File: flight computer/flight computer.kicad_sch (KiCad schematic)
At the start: 16 parts, among them U1 TPS56A37RPAR

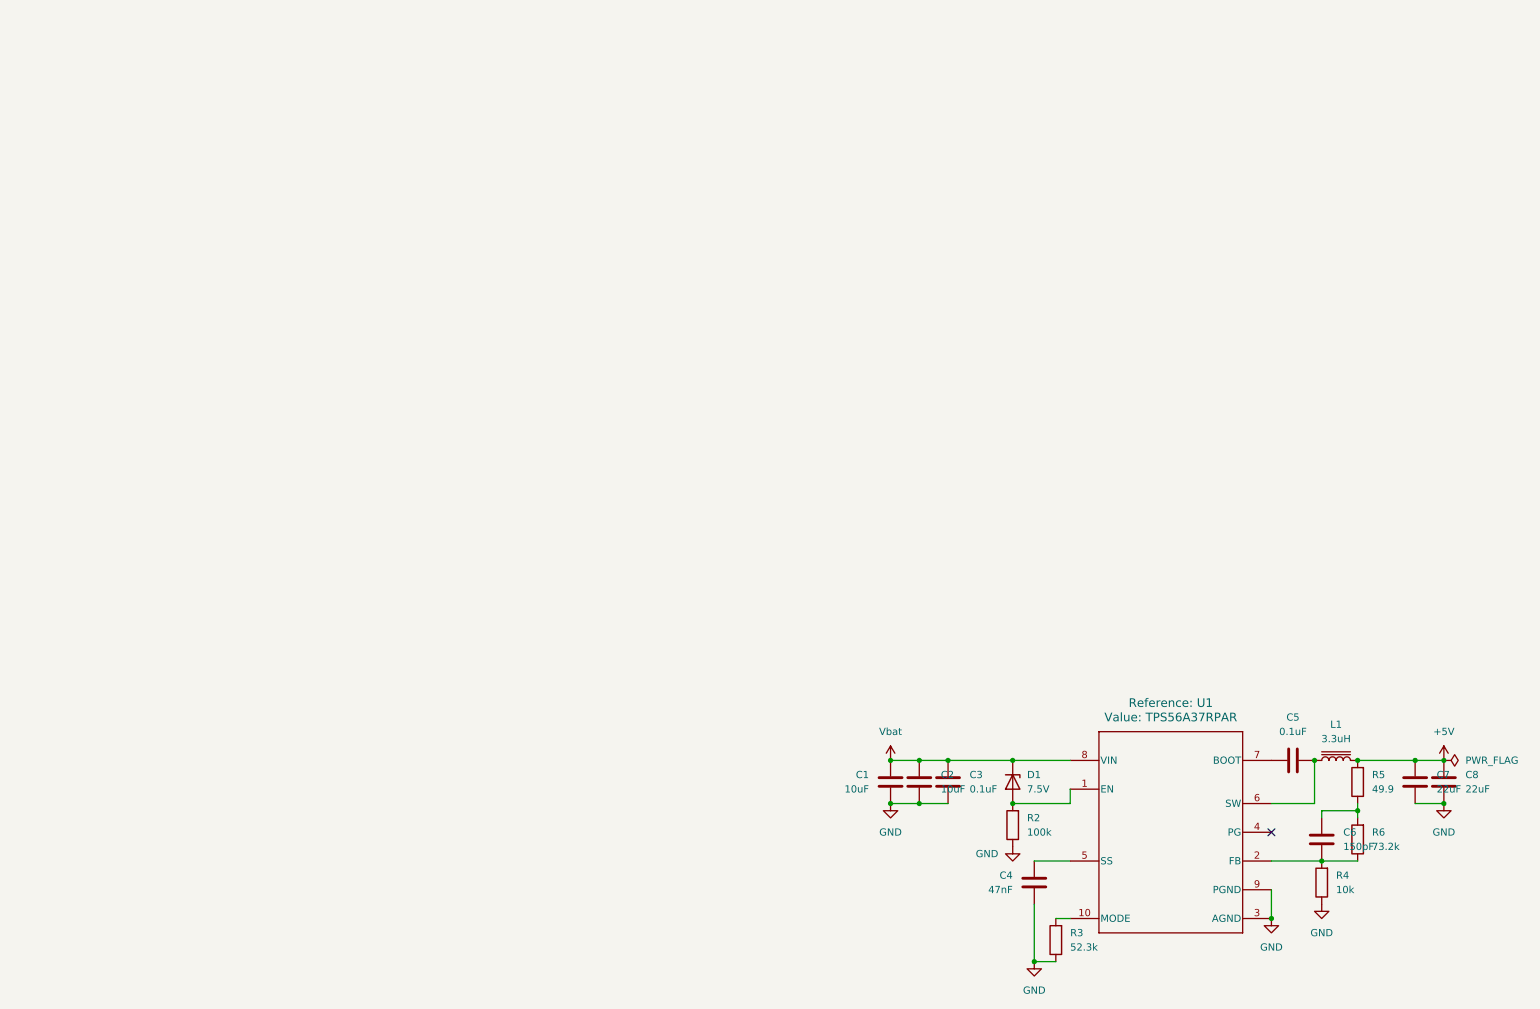
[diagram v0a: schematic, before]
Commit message: BMP581 barometer added
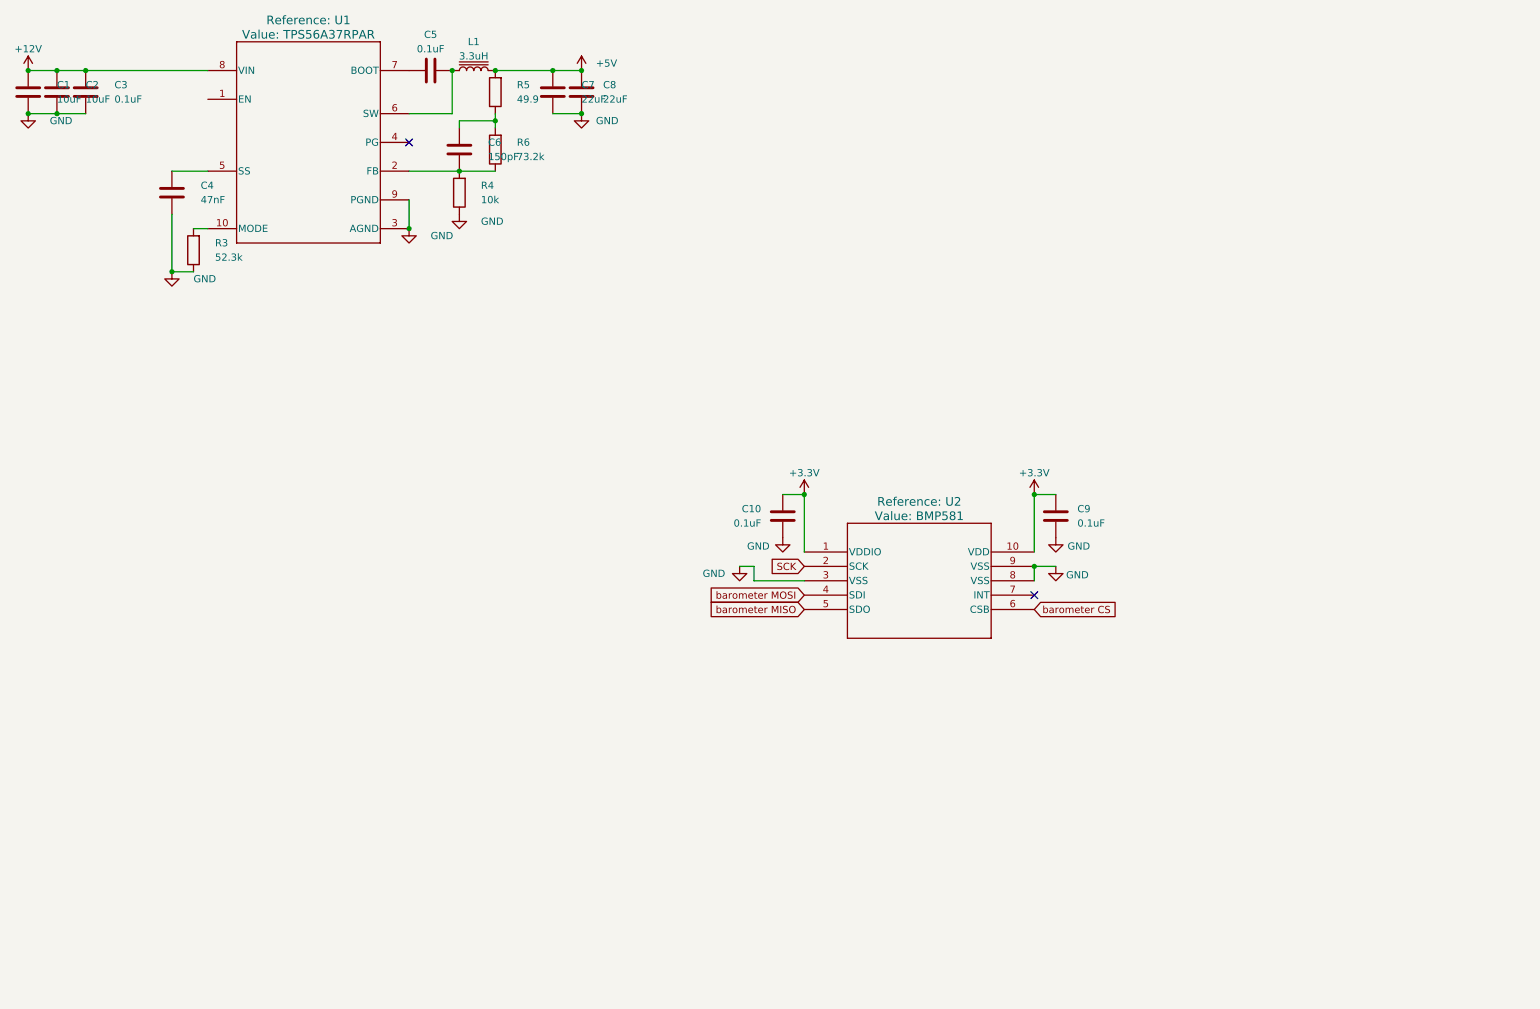
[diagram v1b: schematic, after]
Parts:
- removed D1: 7.5V, symbol Device:D_Zener
- removed R2: 100k, Resistor_SMD:R_0805_2012Metric_Pad1.20x1.40mm_HandSolder, symbol Device:R
- added C10, C9: 0.1uF, Capacitor_SMD:C_0805_2012Metric_Pad1.18x1.45mm_HandSolder, symbol Device:C
- added U2: BMP581, Snapeda:QFN10_BMP581_BOS-L, symbol Snapeda:BMP581
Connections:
- net GND: now also C10.2, C9.2, U2.3 (VSS), U2.8 (VSS), U2.9 (VSS)
- net Vbat renamed +12V
- new net +3.3V: C10.1, C9.1, U2.1 (VDDIO), U2.10 (VDD)
- new net SCK: U2.2 (SCK)
- new net barometer CS: U2.6 (CSB)
- new net barometer MISO: U2.5 (SDO)
- new net barometer MOSI: U2.4 (SDI)
- no-connect marks 1 -> 2
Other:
- moved on the sheet: C1, C2, C3, C4, C5, C6, C7, C8, L1, R3, R4, R5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

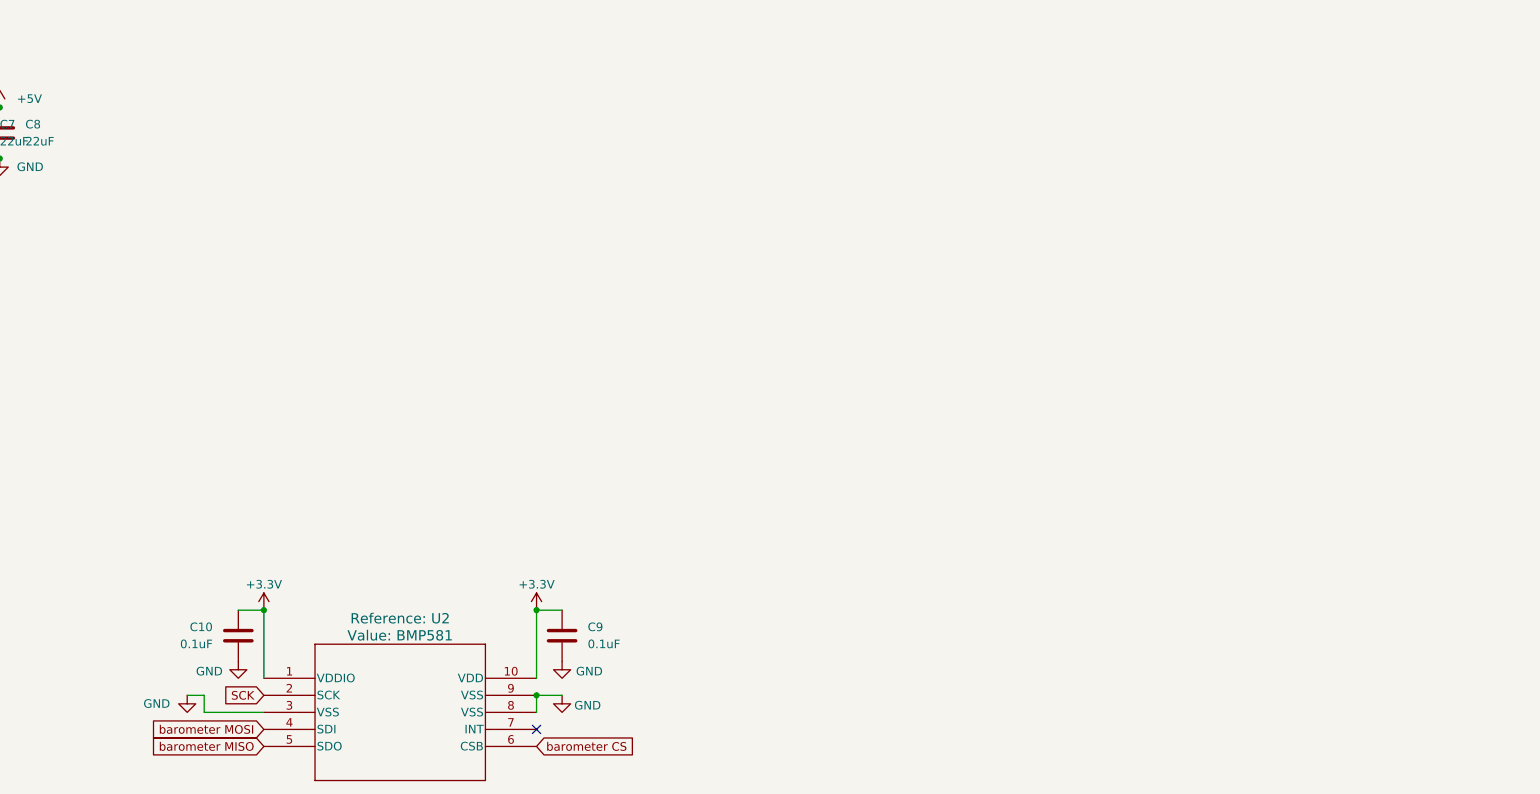
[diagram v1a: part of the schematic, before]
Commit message: BNO086 IMU added
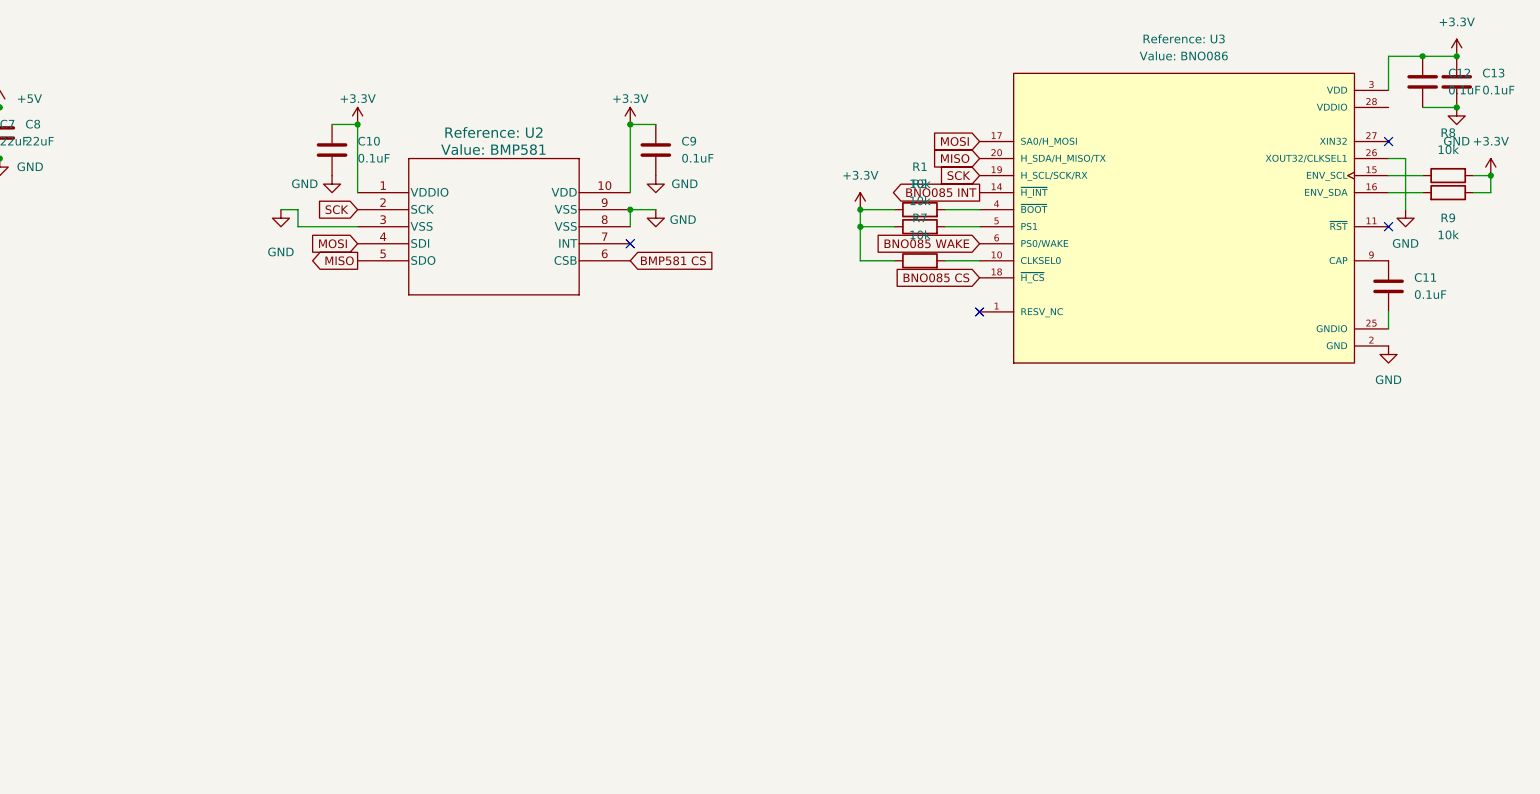
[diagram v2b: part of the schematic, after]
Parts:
- added C11, C12, C13: 0.1uF, Capacitor_SMD:C_0805_2012Metric_Pad1.18x1.45mm_HandSolder, symbol Device:C
- added R1, R2, R7, R8, R9: 10k, Resistor_SMD:R_0805_2012Metric_Pad1.20x1.40mm_HandSolder, symbol Device:R
- added U3: BNO086, Snapeda:IC_BNO086, symbol Snapeda:BNO086
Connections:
- net +3.3V: now also C12.1, C13.1, R1.1, R2.1, R7.1, R8.2, R9.1, U3.3 (VDD)
- net GND: now also C12.2, C13.2, U3.2 (GND), U3.26 (XOUT32/CLKSEL1)
- net SCK: now also U3.19 (H_SCL/SCK/RX)
- net barometer CS renamed BMP581 CS
- net barometer MISO renamed MISO
- net MISO: now also U3.20 (H_SDA/H_MISO/TX)
- net barometer MOSI renamed MOSI
- net MOSI: now also U3.17 (SA0/H_MOSI)
- new net: R7.2, U3.10 (CLKSEL0)
- new net: R2.2, U3.5 (PS1)
- new net: C11.1, U3.9 (CAP)
- new net: C11.2, U3.25 (GNDIO)
- new net: R9.2, U3.16 (ENV_SDA)
- new net: U3.1 (RESV_NC), U3.12 (RESV_NC), U3.13 (RESV_NC), U3.21 (RESV_NC), U3.22 (RESV_NC), U3.23 (RESV_NC), U3.24 (RESV_NC), U3.7 (RESV_NC), U3.8 (RESV_NC)
- new net: R8.1, U3.15 (ENV_SCL)
- new net: R1.2, U3.4 (~{BOOT})
- new net BNO085 CS: U3.18 (~{H_CS})
- new net BNO085 INT: U3.14 (~{H_INT})
- new net BNO085 WAKE: U3.6 (PS0/WAKE)
- no-connect marks 2 -> 5
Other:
- moved on the sheet: C10, C9, Reference: U2

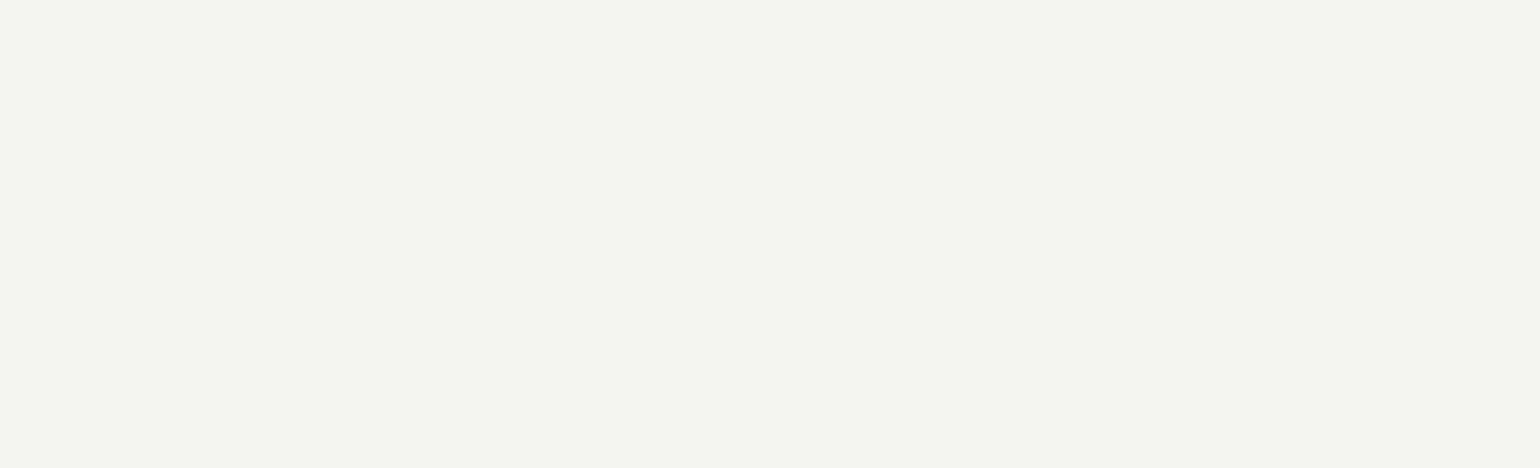
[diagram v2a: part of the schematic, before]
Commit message: BTM9011EP motor controller added
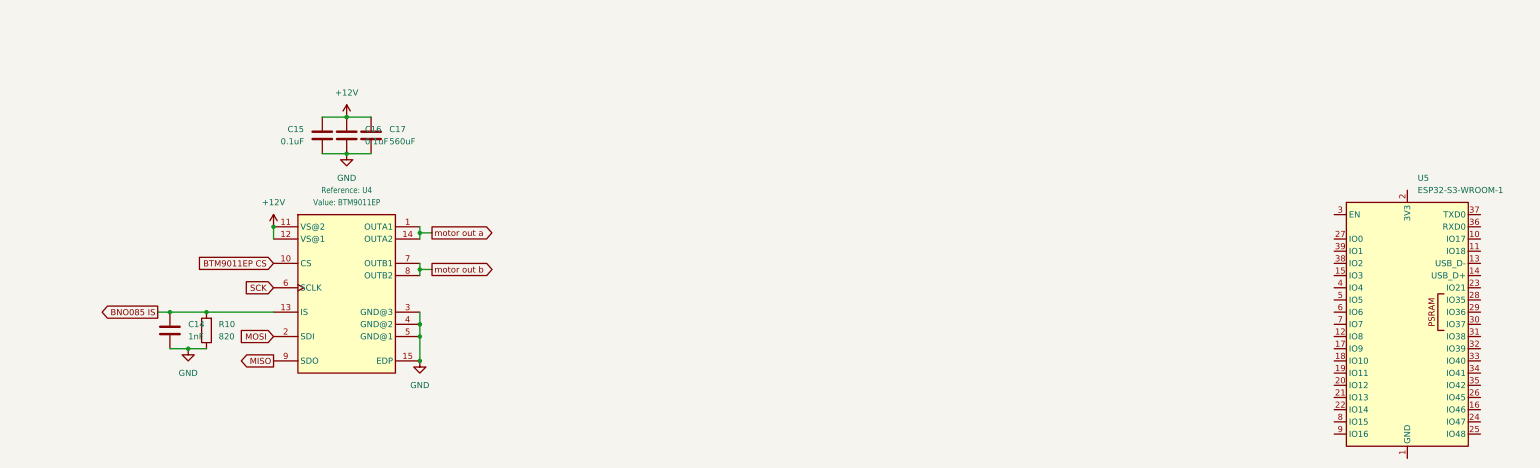
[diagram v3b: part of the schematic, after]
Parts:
- added C14: 1nF, Capacitor_SMD:C_0805_2012Metric_Pad1.18x1.45mm_HandSolder, symbol Device:C
- added C15, C16: 0.1uF, Capacitor_SMD:C_0805_2012Metric_Pad1.18x1.45mm_HandSolder, symbol Device:C
- added C17: 560uF, Capacitor_SMD:C_0805_2012Metric_Pad1.18x1.45mm_HandSolder, symbol Device:C
- added R10: 820, Resistor_SMD:R_0805_2012Metric_Pad1.20x1.40mm_HandSolder, symbol Device:R
- added U4: BTM9011EP, Samacsys:SOP65P600X115-15N, symbol Samacsys:BTM9011EP
- added U5: ESP32-S3-WROOM-1, RF_Module:ESP32-S3-WROOM-1, symbol RF_Module:ESP32-S3-WROOM-1
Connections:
- net +12V: now also C15.1, C16.1, C17.1, U4.11 (VS@2), U4.12 (VS@1)
- net GND: now also C14.2, C15.2, C16.2, C17.2, R10.1, U4.15 (EDP), U4.3 (GND@3), U4.4 (GND@2), U4.5 (GND@1)
- net MISO: now also U4.9 (SDO)
- net MOSI: now also U4.2 (SDI)
- net SCK: now also U4.6 (SCLK)
- new net: U5.1 (GND), U5.40 (GND), U5.41 (GND)
- new net BNO085 IS: C14.1, R10.2, U4.13 (IS)
- new net BTM9011EP CS: U4.10 (CS)
- new net motor out a: U4.1 (OUTA1), U4.14 (OUTA2)
- new net motor out b: U4.7 (OUTB1), U4.8 (OUTB2)

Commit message: MAX M10S GNSS added
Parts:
- removed U5: ESP32-S3-WROOM-1, RF_Module:ESP32-S3-WROOM-1, symbol RF_Module:ESP32-S3-WROOM-1
- added C18: 10nF, Capacitor_SMD:C_0805_2012Metric_Pad1.18x1.45mm_HandSolder, symbol Device:C
- added C19: 47pF, Capacitor_SMD:C_0805_2012Metric_Pad1.18x1.45mm_HandSolder, symbol Device:C
- added J1: SMA-J-P-H-ST-EM1, Snapeda:SAMTEC_SMA-J-P-H-ST-EM1, symbol Snapeda:SMA-J-P-H-ST-EM1
- added L2: 27uH, Inductor_SMD:L_0805_2012Metric_Pad1.05x1.20mm_HandSolder, symbol Device:L
- added Q1: BSS138, Package_TO_SOT_SMD:SOT-23-3, symbol Simulation_SPICE:NMOS
- added Q2: BSS84, Package_TO_SOT_SMD:SOT-23-3, symbol Simulation_SPICE:PMOS
- added R11: 100k, Resistor_SMD:R_0805_2012Metric_Pad1.20x1.40mm_HandSolder, symbol Device:R
- added R12: 10, Resistor_SMD:R_0805_2012Metric_Pad1.20x1.40mm_HandSolder, symbol Device:R
- added U5: RP2354B, Package_DFN_QFN:QFN-80-1EP_10x10mm_P0.4mm_EP3.4x3.4mm, symbol MCU_RaspberryPi:RP2354B
- added U6: MAX-M10S-00B, Snapeda:XCVR_MAX-M10S-00B, symbol Snapeda:MAX-M10S-00B
- added U7: SX1262IMLTRT, Snapeda:QFN50P400X400X100-25N, symbol Snapeda:SX1262IMLTRT
- added U8: VND9025AJTR, Snapeda:IC_POWERSSO-16_STM-L, symbol Snapeda:VND9025AJTR
- added U9: 74LVC1G07GW_125, Snapeda:IC_74LVC1G07GW_125, symbol Snapeda:74LVC1G07GW_125
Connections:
- net +3.3V: now also U6.7 (V_IO), U6.8 (VCC)
- net GND: now also C18.2, J1.2_1, J1.2_2, J1.3_1, J1.3_2, Q1.3 (S), U6.1 (GND), U6.10 (GND__1), U6.12 (GND__2), U7.2 (GND), U7.20 (GND), U7.5 (GND), U7.8 (GND), U9.3 (GND)
- net BNO085 CS renamed BNO086 CS
- net BNO085 INT renamed BNO086 INT
- net BNO085 IS renamed BTM9011EP IS
- net BNO085 WAKE renamed BNO086 WAKE
- new net: C18.1, L2.2, R12.1, U9.2 (A)
- new net: U6.5 (EXTINT), U9.4 (Y)
- new net: C19.1, J1.1, L2.1
- new net: C19.2, U6.11 (RF_IN)
- new net: Q1.1 (D), Q2.2 (G), R11.1
- new net: Q2.1 (D), R12.2
- new net: U5.10 (DVDD), U5.32 (DVDD), U5.51 (DVDD)
- new net: U5.15 (IOVDD), U5.24 (IOVDD), U5.29 (IOVDD), U5.41 (IOVDD), U5.5 (IOVDD), U5.50 (IOVDD), U5.60 (IOVDD), U5.76 (IOVDD)
- new net: Q1.2 (G), U6.13 (LNA_EN)
- new net MAX M10S RESET: U6.9 (~{RESET})
- new net MAX M10S RX: U6.3 (RXD)
- new net MAX M10S TIMEPULSE: U6.4 (TIMEPULSE)
- new net MAX M10S TX: U6.2 (TXD)
- new net VCC_RF: Q2.3 (S), R11.2, U6.14 (VCC_RF), U9.5 (VCC)
- no-connect marks 5 -> 11
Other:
- moved on the sheet: C14, C15, C16, C17, R10, Reference: U4

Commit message: SX1262 added
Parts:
- removed U7: SX1262IMLTRT, Snapeda:QFN50P400X400X100-25N, symbol Snapeda:SX1262IMLTRT
- added C20, C21: 10nF, Capacitor_SMD:C_0805_2012Metric_Pad1.18x1.45mm_HandSolder, symbol Device:C
- added IC1: 114993390, Samacsys:114993390, symbol Samacsys:114993390
- added J2: SMA-J-P-H-ST-EM1, Snapeda:SAMTEC_SMA-J-P-H-ST-EM1, symbol Snapeda:SMA-J-P-H-ST-EM1
- added L3: 27uH, Inductor_SMD:L_0805_2012Metric_Pad1.05x1.20mm_HandSolder, symbol Device:L
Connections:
- net +3.3V: now also IC1.8 (VCC)
- net GND: now also C20.2, C21.2, IC1.10 (GND_2), IC1.7 (GND_1), J2.2_1, J2.2_2, J2.3_1, J2.3_2
- net MISO: now also IC1.2 (MISO)
- net MOSI: now also IC1.3 (MOSI)
- net SCK: now also IC1.4 (SCK)
- new net: C20.1, J2.1, L3.2
- new net: C21.1, IC1.9 (ANT), L3.1
- new net SX1262 BUSY: IC1.11 (BUSY)
- new net SX1262 CS: IC1.6 (NSS)
- new net SX1262 INT: IC1.12 (DIO1)
- new net SX1262 RESET: IC1.5 (NRST)
- new net SX1262 RF_SW: IC1.1 (RF_SW_)
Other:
- moved on the sheet: C18, C19, L2, Q1, Q2, R11, R12, Reference: J1, Reference: U6, Reference: U9
